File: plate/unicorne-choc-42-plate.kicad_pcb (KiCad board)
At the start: 2 copper layers, 299.9 x 118.8 mm, 12 parts

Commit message: Solid 42- and 36-key switch plates for MX and Choc; re-export everything
Plates no longer have break lines. Each switch type gets a 42-key plate and a
36-key plate cut where the PCB snaps off its outer columns, with rounded
corners and only the holes whose screw head fits. PCB gerbers, STEP and
renders regenerated.

Co-Authored-By: Claude Opus 5.5 <noreply@anthropic.com>
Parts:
- removed MB1, MB2: mouse bites, 
- moved H6 8.05 mm to (263.2, 100.0)
- moved H1 2.57 mm to (133.0, 70.3)
- moved H5 2.02 mm to (224.0, 73.6)
- moved H4 1.80 mm to (76.5, 58.8)
- moved H2 1.52 mm to (96.8, 100.0)
- moved H8 1.25 mm to (283.0, 59.1)
- moved H3 0.50 mm to (134.9, 121.6)
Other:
- outline, holes or cut-outs redrawn
- board text added: "unicorne CHOC 42"
- board text removed: "unicorne MX plate"

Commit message: Halves closer, trackpad on the case; GND repair in the router; re-export
- The trackpad sits on the case above the board, so it may cover the
  nice!nano. layout.py places it where its keycap keep-out lets the halves
  come closest: each half moves 3.25 mm inward and the board is 293.4 mm wide
  (was 299.9). The parts below it follow; it has no 3D model on the board.
- The level shifter group (U2, C2, JP3) moves down, clear of the inner
  column, which now comes within ~6.5 mm of the headers.
- J3/J4 headers have no 3D model (bare holes in the renders and STEP).
- finish_route.py: jitters the routing order between attempts, and repairs
  GND the pours left cut off (tools/gnd_repair.py: a via where the pocket
  overlaps the main ground, else rip up the net boxing it in and reroute).
- Both boards rerouted: DRC 0 unconnected, schematic parity 0, every pin,
  the matrix, the LED chain and one GND group verified. Gerbers, STEP,
  renders and all four plates regenerated. copper_sliver (a thin point in a
  GND pour) counts as harmless for the gerber export.

Co-Authored-By: Claude Opus 5.5 <noreply@anthropic.com>
Claude-Session: https://claude.ai/code/session_01D39ubfTYtq6FMvNmmbStTo
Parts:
- moved H5 6.25 mm to (217.7, 73.6)
- moved H6 6.25 mm to (257.0, 100.0)
- moved H7 6.25 mm to (219.3, 121.6)
- moved H8 6.25 mm to (276.8, 59.1)
- moved H10 3.59 mm to (191.0, 131.6)
- moved H9 3.59 mm to (163.0, 131.6)
- moved H1 0.25 mm to (133.3, 70.3)
- moved H2 0.25 mm to (97.0, 100.0)
- moved H3 0.25 mm to (135.2, 121.6)
- moved H4 0.25 mm to (76.7, 58.8)
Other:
- board size 299.9 x 118.8 mm -> 293.4 x 118.8 mm

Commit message: Plates: openings for the nice!nano (through the top edge) and the reset switch
Both from where the PCB has them, 0.5 mm clearance, 0.8 mm corner radius. The
nano opening joins the trackpad opening; all four plates pass DRC.

Co-Authored-By: Claude Opus 5.5 <noreply@anthropic.com>
Claude-Session: https://claude.ai/code/session_01D39ubfTYtq6FMvNmmbStTo
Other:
- outline, holes or cut-outs redrawn

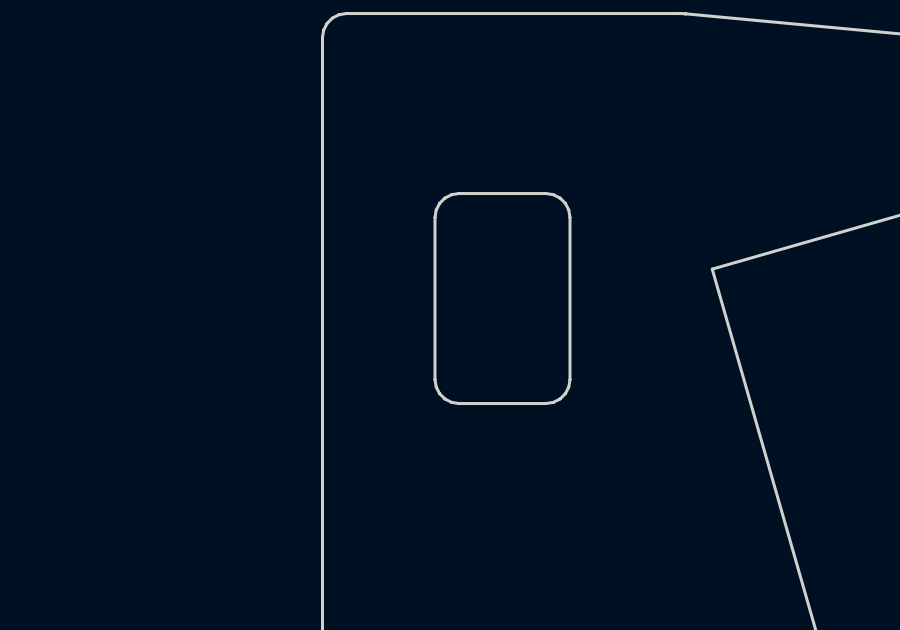
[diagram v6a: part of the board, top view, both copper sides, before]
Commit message: Route both boards with KiCadRoutingTools; no vias in pads
tools/krt_route.py: fixed lanes, then KiCadRoutingTools 0.23.7 for every other
signal at standard JLCPCB sizes (0.6/0.3 vias, 0.2 tracks) with no via in or next
to a pad, own net's included; the maze router for any net it could only finish
with undersized vias; GND pours and stitching; its plane repair; then any via
touching a pad is removed. The tools relax the project's rules on disk: ours are
put back.

MX lanes: LED_VDD's jog across a break line moves from 5.5 to 4.5 mm off the
line. At 5.5 it boxed in the outer-column LED DIN pads, so 8 LED data links had
no room for a via outside a pad. Lane-only board: no DRC errors.

Stitching vias (finish_route.stitch) and our maze router stay off SMD pads too.
The previous MX board had 82 vias in pads, now none on either board.

MX: U2 pad 3 (GND) is boxed in by LED_DIN; joined by hand with a via between
pads 3 and 4 (noted in the README).

Both boards: DRC 0 unconnected, 0 copper violations, schematic parity clean;
all 482 schematic pins, 42 keys and the 54-LED chain check out pin by pin.
Waves, LED map, plates, gerbers, STEP and renders regenerated.

Co-Authored-By: Claude Opus 5.5 <noreply@anthropic.com>
Claude-Session: https://claude.ai/code/session_01D39ubfTYtq6FMvNmmbStTo
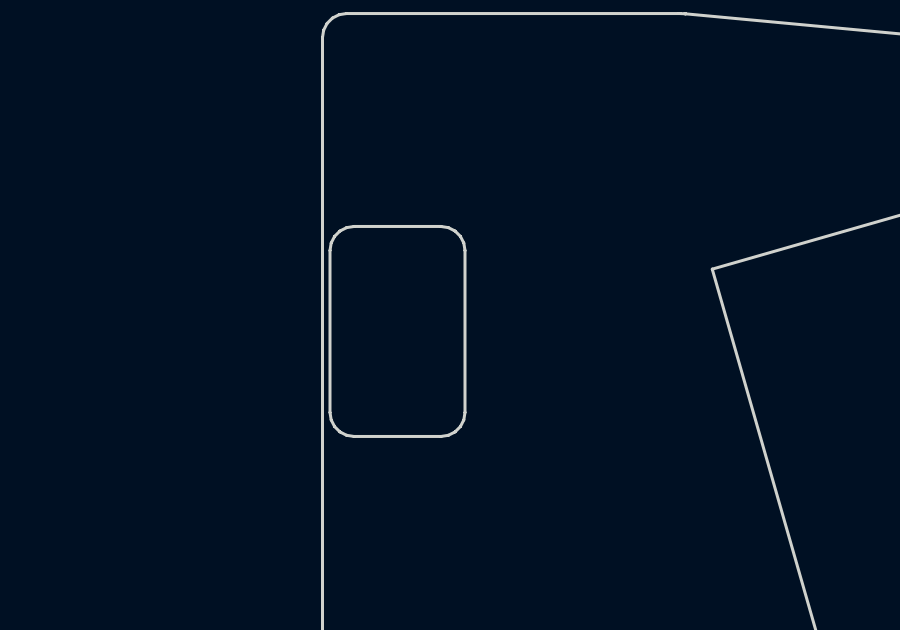
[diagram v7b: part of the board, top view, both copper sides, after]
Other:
- outline, holes or cut-outs redrawn
